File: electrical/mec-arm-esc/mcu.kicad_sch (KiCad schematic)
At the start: 18 parts, among them SW1 SH-1808SN-250GF, SW2 SH-1808SN-250GF, U2 STM32G474RET3, X1 NX3225GD-8MHZ-STD-CRA-3

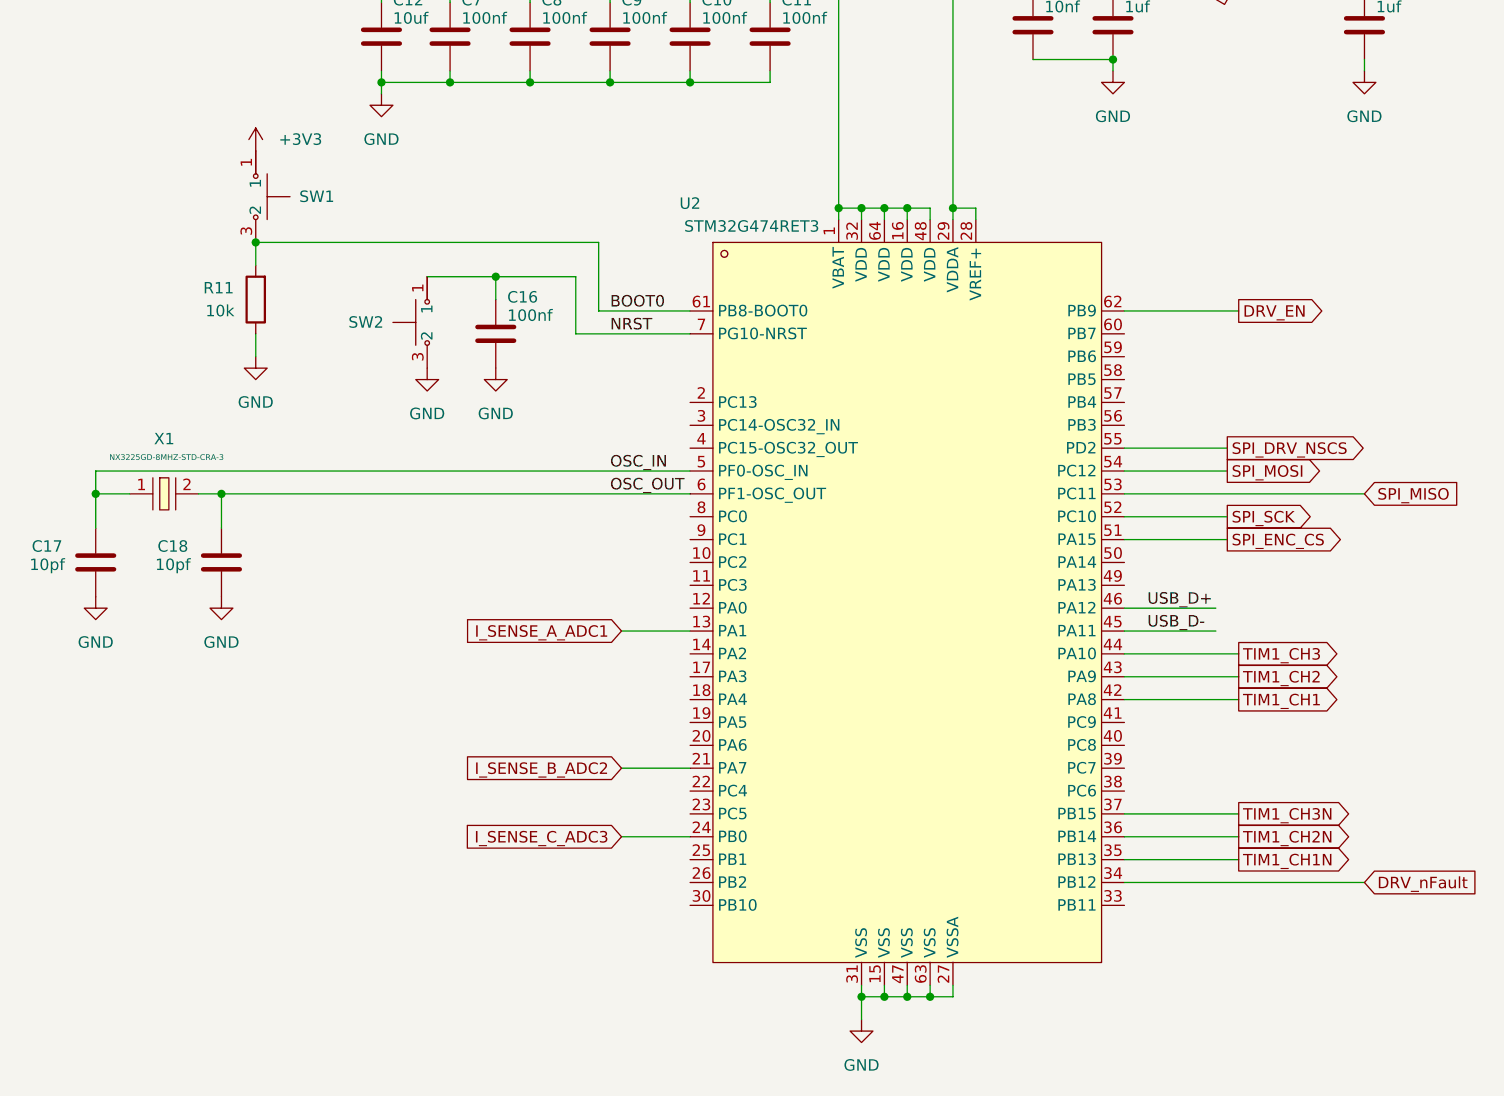
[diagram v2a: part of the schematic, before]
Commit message: Changed the components in all the drawings to reflect the new library, and added vbus sensing
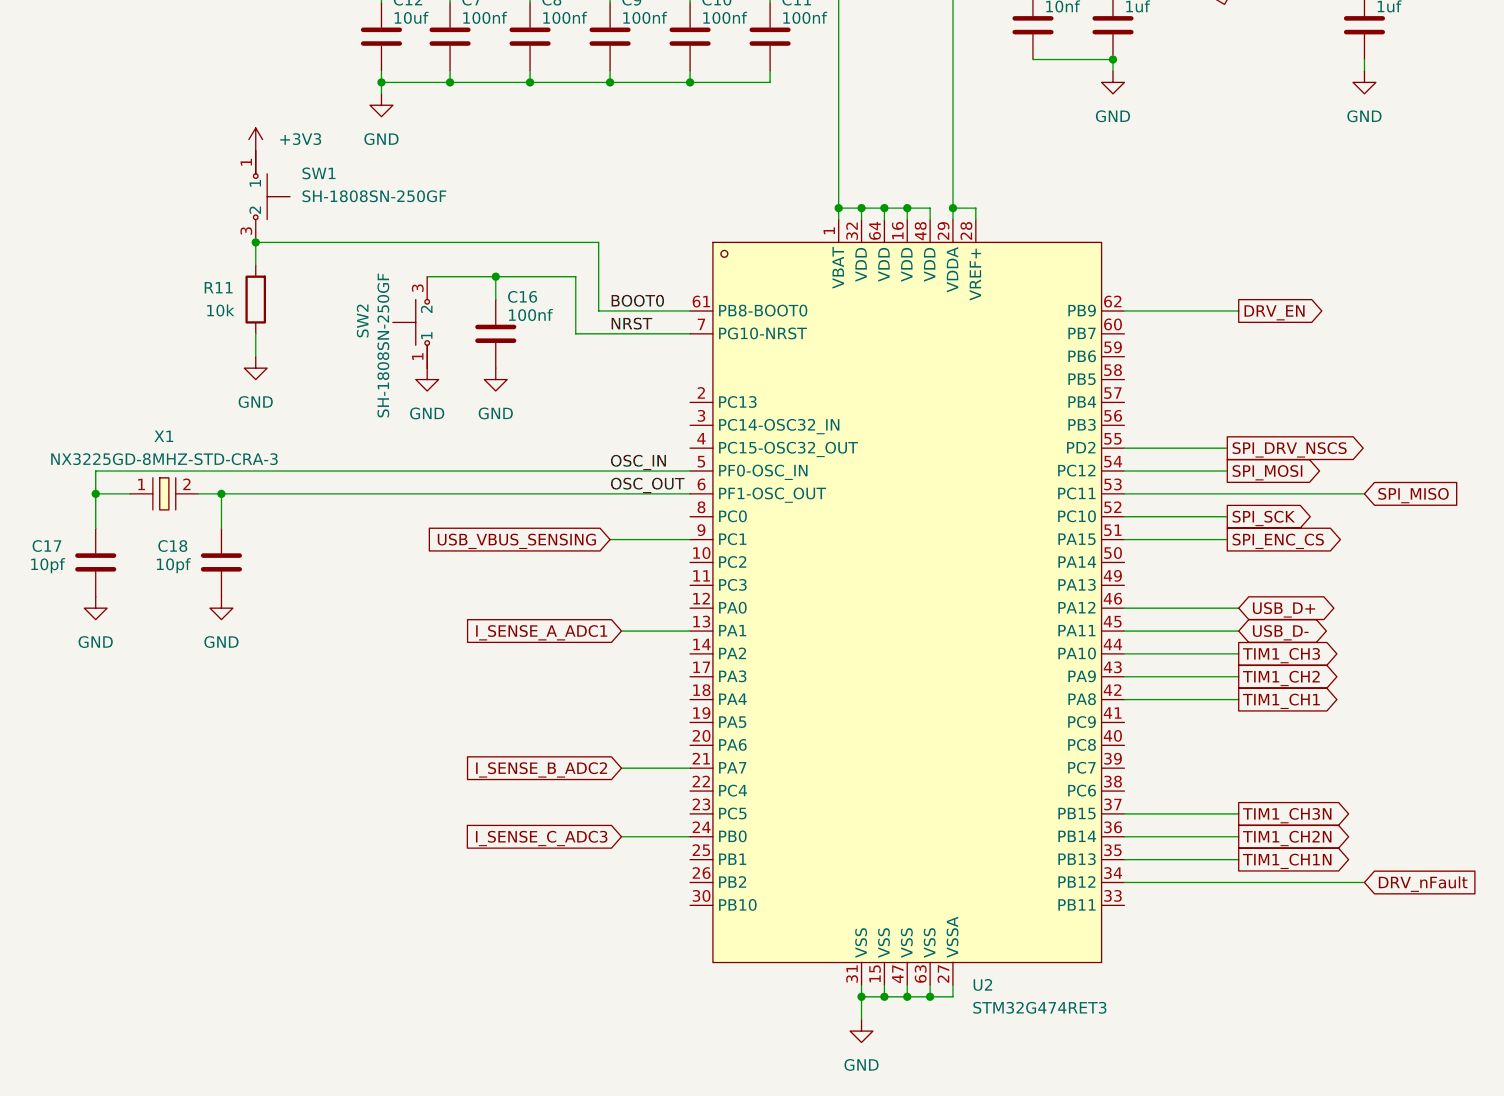
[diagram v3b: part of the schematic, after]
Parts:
- SW1, SW2: footprint EasyEDA:SW-SMD_4P-L4.2-W3.4-P2.15-LS5.2 -> core:SW-SMD_4P-L4.2-W3.4-P2.15-LS5.2
- U2: footprint EasyEDA:LQFP-64_L10.0-W10.0-P0.50-LS12.0-BL -> mcu:LQFP-64_L10.0-W10.0-P0.50-LS12.0-BL
- X1: footprint EasyEDA:OSC-SMD_2P-L3.2-W2.5 -> core:OSC-SMD_2P-L3.2-W2.5
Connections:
- net GND: now also SW2.1; no longer SW2.3 (2)
- net NRST: now also SW2.3 (2); no longer SW2.1
- net USB_VBUS_SENSING: now reaches U2.9 (PC1)

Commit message: Added peripheral systems, and corresponding mcu entries
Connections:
- net VBUS_SENSE: now reaches U2.12 (PA0)
- net TEMP_SENSE: now reaches U2.22 (PC4)
- net UART_TX: now reaches U2.30 (PB10)
- net UART_RX: now reaches U2.33 (PB11)
- net FDCAN_RX: now reaches U2.56 (PB3)
- net FDCAN_TX: now reaches U2.57 (PB4)
- net ENC_Z: now reaches U2.58 (PB5)
- net ENC_A: now reaches U2.59 (PB6)
- net ENC_B: now reaches U2.60 (PB7)

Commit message: Schematic Done, review 1
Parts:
- removed C17, C18: 10pf, symbol Device:C
- removed FB1: 600 Ohms @ 100MHz, symbol Device:FerriteBead
- removed X1: NX3225GD-8MHZ-STD-CRA-3, core:OSC-SMD_2P-L3.2-W2.5, symbol core:NX3225GD-8MHZ-STD-CRA-3
- added FB1: BLM15BX601SN1D, core:L0402, symbol core:BLM15BX601SN1D
- added R46: 220, symbol Device:R
- added X1: CSTNE8M00GH5C000R0, core:OSC-SMD_3P-L3.2-W1.3-P1.20-L, symbol core:CSTNE8M00GH5C000R0
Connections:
- net +3V3: now also FB1.2
- net +3V3A: now also FB1.1
- net GND: now also X1.2 (GND)
- net OSC_IN: now also X1.1 (OSC1)
- net OSC_OUT: now also R46.1
- net ADC_FORCE2+: now reaches U2.10 (PC2)
- net ADC_FORCE2-: now reaches U2.11 (PC3)
- net ADC_FORCE1+: now reaches U2.14 (PA2)
- net ADC_FORCE1-: now reaches U2.17 (PA3)
- net DAC_OUT1: now reaches U2.18 (PA4)
- net LED_DEBUG2: now reaches U2.19 (PA5)
- net LASER_CTRL: now reaches U2.2 (PC13)
- net FAN_CTRL: now reaches U2.3 (PC14-OSC32_IN)
- net GPIO_EXT1: now reaches U2.38 (PC6)
- net GPIO_EXT2: now reaches U2.39 (PC7)
- net SWDIO: now reaches U2.49 (PA13)
- net SWCLK: now reaches U2.50 (PA14)
- net LED_DEBUG1: now reaches U2.8 (PC0)
- new net: R46.2, X1.3 (OSC2)
- no-connect marks 0 -> 7
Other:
- note added: "MCU"
- moved on the sheet: C10, C11, C12, C13, C14, C15, C16, C7, C8, C9, R11, SW1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

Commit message: Done placement, starting routing
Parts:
- removed R46: 220, symbol Device:R
- removed X1: CSTNE8M00GH5C000R0, core:OSC-SMD_3P-L3.2-W1.3-P1.20-L, symbol core:CSTNE8M00GH5C000R0
- added C17, C18: 16pF, core:C_0603, symbol Device:C
- added X1: 3225 8M 12PF 10PPM, core:CRYSTAL-SMD_4P-L3.2-W2.5-BL, symbol core:32258M12PF10PPM
- C10, C11, C13, C14, C15, C16, C7, C8, C9: footprint (none) -> core:C_0603
- C12: footprint (none) -> core:C_0805
- R11: footprint (none) -> core:R_0603
- U2: footprint mcu:LQFP-64_L10.0-W10.0-P0.50-LS12.0-BL -> my_mcu:LQFP-64_L10.0-W10.0-P0.50-LS12.0-BL
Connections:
- net +3V3: now also SW1.2
- net GND: now also SW2.3 (2), SW2.4, C17.2, C18.2, X1.2 (GND), X1.4 (GND); no longer SW2.1
- net NRST: now also SW2.1, SW2.2; no longer SW2.3 (2)
- net OSC_IN: now also C18.1, X1.1
- net OSC_OUT: now also C17.1, X1.3
- net GPIO_EXT3: now reaches U2.40 (PC8)
- no-connect marks 7 -> 6

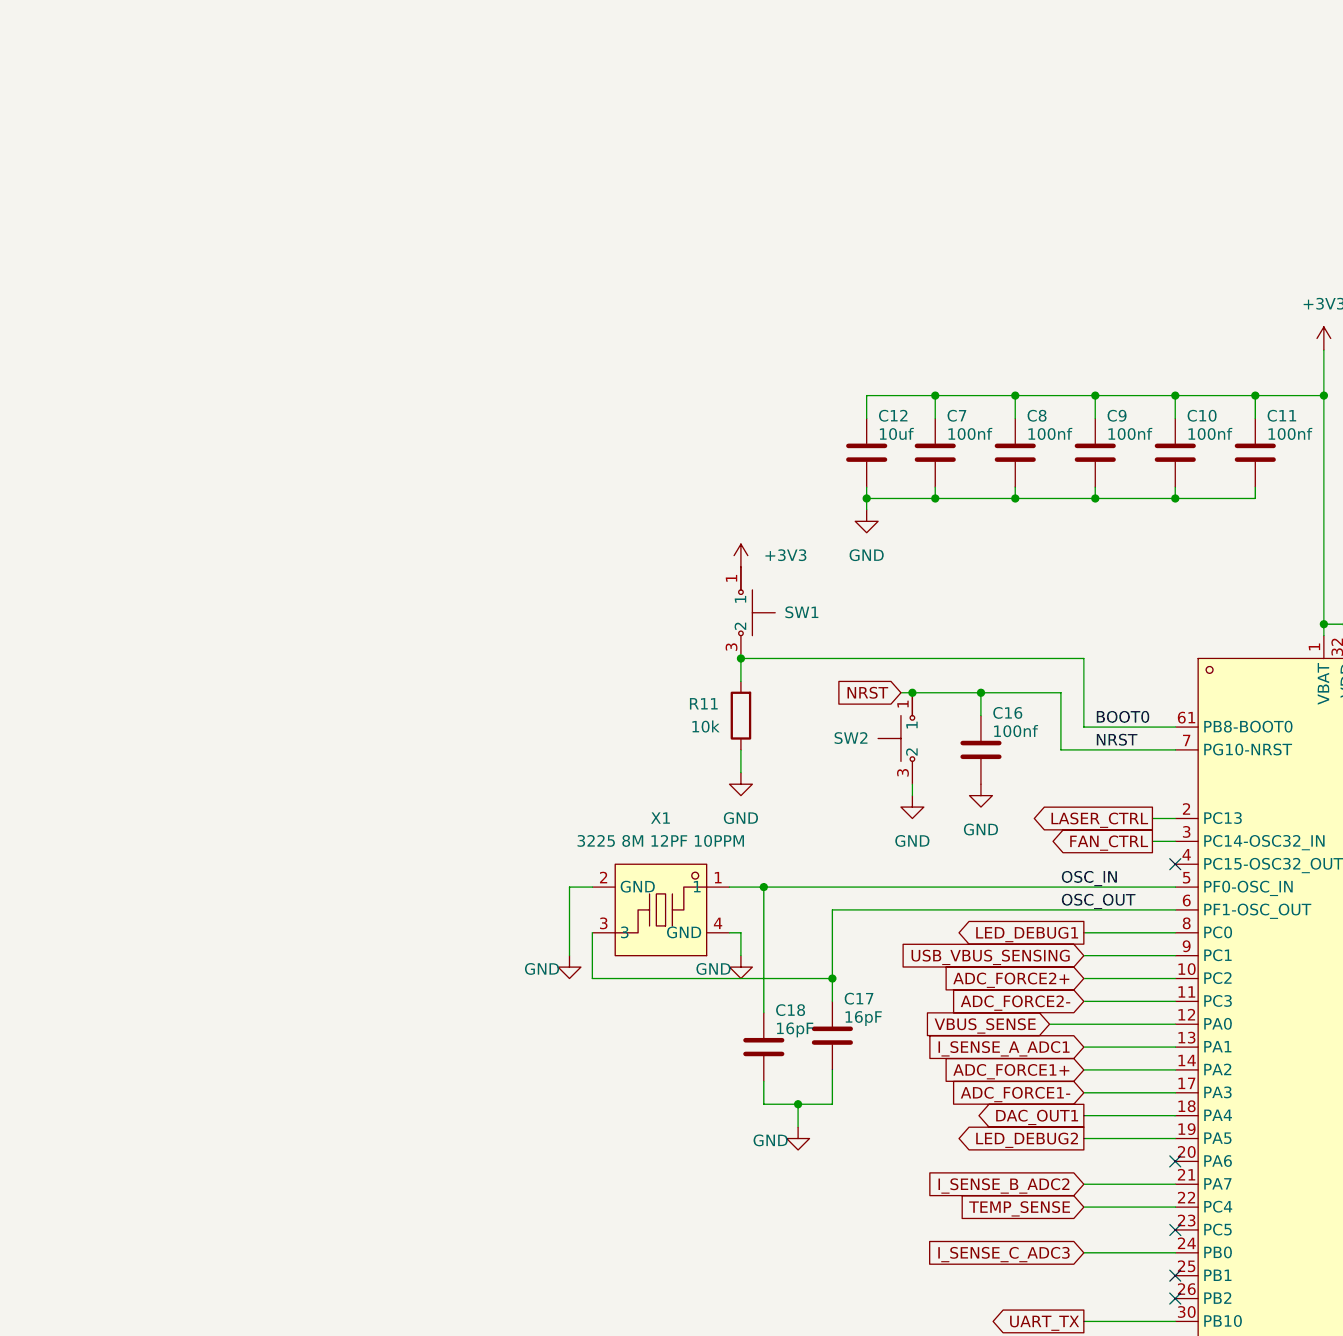
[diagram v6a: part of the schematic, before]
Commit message: All signal routing finishes, power and planes not yet
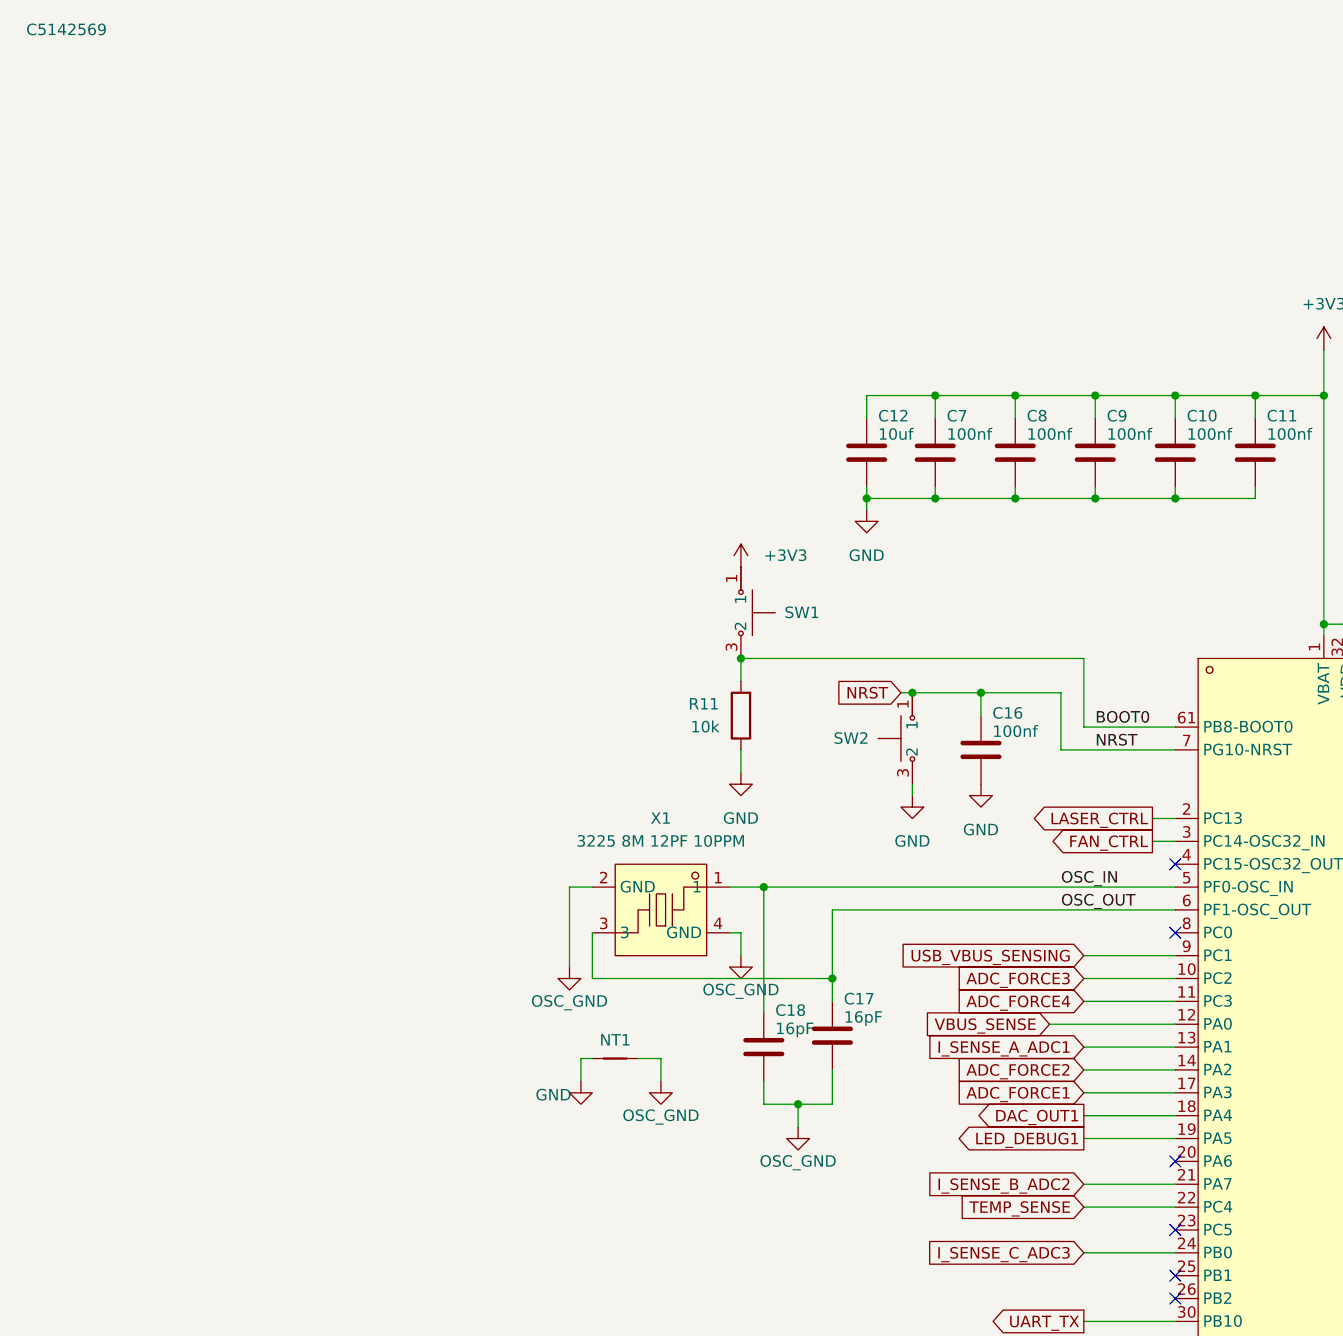
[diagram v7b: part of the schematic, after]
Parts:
- added NT1: NetTie_2, NetTie:NetTie-2_SMD_Pad0.5mm, symbol Device:NetTie_2
- C10, C11, C16, C7, C8, C9: LCSC Part (none) -> C108079
- C12: LCSC Part (none) -> C711098
- C13: LCSC Part (none) -> C519406
- C14, C15: LCSC Part (none) -> C106248
- C17, C18: footprint core:C_0603 -> Capacitor_SMD:C_0402_1005Metric; LCSC Part (none) -> C5142569
- R11: LCSC Part (none) -> C98220
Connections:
- net LED_DEBUG2 is gone; now on net LED_DEBUG1: U2.19 (PA5)
- net GND: now also NT1.1; no longer C17.2, C18.2, X1.2 (GND), X1.4 (GND)
- net LED_DEBUG1: no longer U2.8 (PC0)
- net ADC_FORCE1+ renamed ADC_FORCE2
- net ADC_FORCE1- renamed ADC_FORCE1
- net ADC_FORCE2+ renamed ADC_FORCE3
- net ADC_FORCE2- renamed ADC_FORCE4
- new net OSC_GND: C17.2, C18.2, NT1.2, X1.2 (GND), X1.4 (GND)
- no-connect marks 6 -> 7
